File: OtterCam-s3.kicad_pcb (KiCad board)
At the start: 4 copper layers, 49.8 x 49.8 mm, 159 parts, among them J1 UART, J2 SD, J3 USB, J4 RJ45, J5 MIPI, J6 LENS, Q1 DTA114YKA, SW1 RST, U1 AllWinner-S3(FBGA-234), U2 AXP209(QFN-48), U3 SY8089AAAC, U4 AP6236, Y1 32.768kHz, Y2 24MHz, Y3 26MHz

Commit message: fixed silkscreen
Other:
- board text added: "OtterCam-s3 Jana Marie Hemsing @JanHenrikH 2021 github.com/Jana-Marie/OtterCam-s3"
- board text removed: "OtterCam-s3 Jan Henrik Hemsing @JanHenrikH 2021 github.com/Jan--Henrik/OtterCam-s3"
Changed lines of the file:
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@@
   )
   (setup
-    (last_trace_width 1)
+    (last_trace_width 0.127)
     (user_trace_width 0.127)
     (user_trace_width 0.2)
@@
       (drillshape 0)
       (scaleselection 1)
-      (outputdirectory "gerber/"))
+      (outputdirectory "gerber_v1.1/"))
   )
   (net 0 "")
@@
     )
   )
-  (gr_text "OtterCam-s3\nJan Henrik Hemsing\n@JanHenrikH 2021\ngithub.com/Jan--Henrik/OtterCam-s3" (at 75 92) (layer B.SilkS)
+  (gr_text "OtterCam-s3\nJana Marie Hemsing\n@JanHenrikH 2021\ngithub.com/Jana-Marie/OtterCam-s3" (at 75 92) (layer B.SilkS)
     (effects (font (size 1.1 1.1) (thickness 0.13)) (justify mirror))
   )

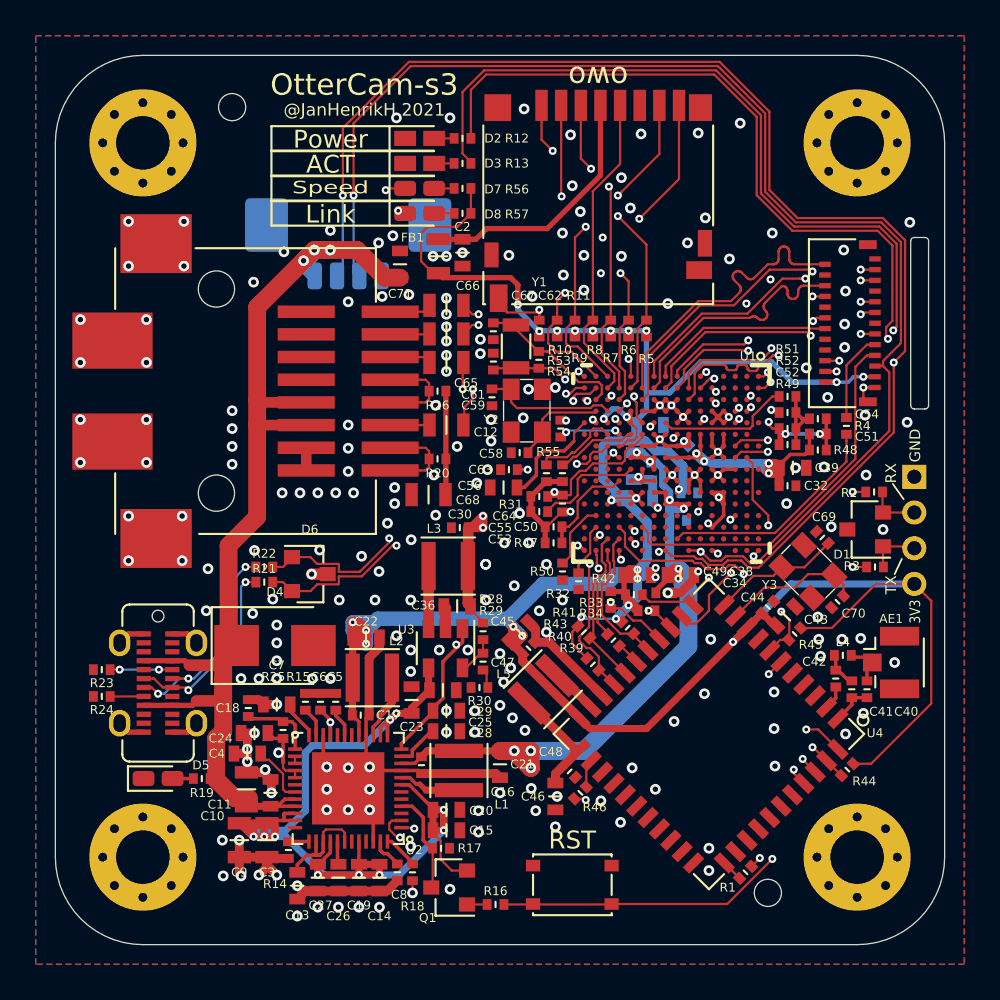
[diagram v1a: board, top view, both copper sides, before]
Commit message: updated to kicad 6
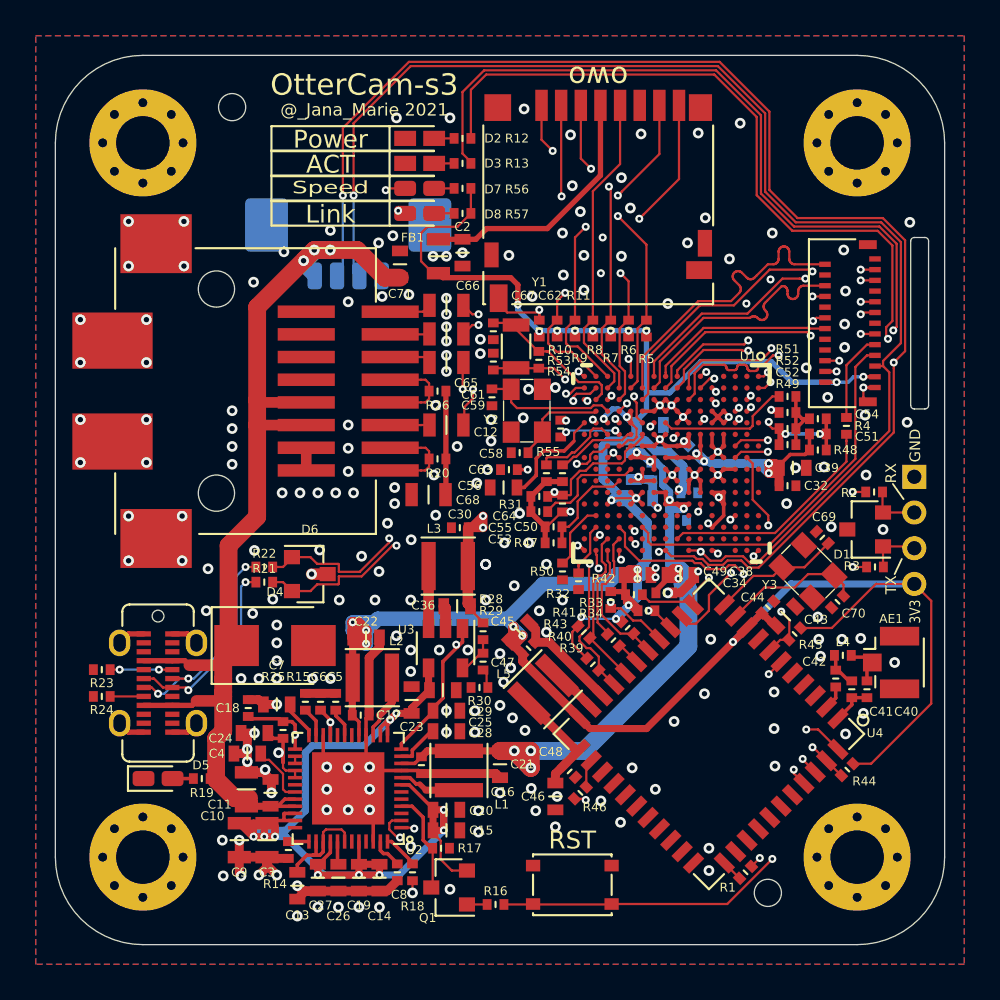
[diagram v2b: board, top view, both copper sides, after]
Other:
- net class Default removed
- board text added: "@_Jana_Marie 2021"
- board text added: "OtterCam-s3 Jana Marie Hemsing @_Jana_Marie 2021 github.com/Jana-Marie/OtterCam-s3"
- board text removed: "@JanHenrikH 2021"
- board text removed: "OtterCam-s3 Jana Marie Hemsing @JanHenrikH 2021 github.com/Jana-Marie/OtterCam-s3"

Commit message: updated project and board files
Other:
- board text added: "Jana Marie 2023"
- board text added: "OtterCam-s3 Jana Marie Hemsing @jana@mystical.garden 2023 github.com/Jana-Marie/OtterCam-s3"
- board text removed: "@_Jana_Marie 2021"
- board text removed: "OtterCam-s3 Jana Marie Hemsing @_Jana_Marie 2021 github.com/Jana-Marie/OtterCam-s3"
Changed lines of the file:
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@@
       (drillshape 0)
       (scaleselection 1)
-      (outputdirectory "gerber_v1.1/")
+      (outputdirectory "gerber_v1.1.1/")
     )
   )
@@
   (gr_line (start 99 60.5) (end 99 69.7) (layer "Edge.Cuts") (width 0.05))
   (gr_line (start 98.8 60.3) (end 98.2 60.3) (layer "Edge.Cuts") (width 0.05))
-  (gr_text "OtterCam-s3\nJana Marie Hemsing\n@_Jana_Marie 2021\ngithub.com/Jana-Marie/OtterCam-s3" (at 75 92) (layer "B.SilkS")
+  (gr_text "OtterCam-s3\nJana Marie Hemsing\n@jana@mystical.garden 2023\ngithub.com/Jana-Marie/OtterCam-s3" (at 75 92) (layer "B.SilkS")
     (effects (font (size 1.1 1.1) (thickness 0.13)) (justify mirror))
   )
@@
     (effects (font (size 1 1) (thickness 0.12)))
   )
-  (gr_text "@_Jana_Marie 2021" (at 67.4 53.15) (layer "F.SilkS")
+  (gr_text "Jana Marie 2023" (at 67.4 53.15) (layer "F.SilkS")
     (effects (font (size 0.7 0.7) (thickness 0.1)))
   )
